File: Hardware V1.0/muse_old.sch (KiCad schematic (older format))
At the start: 47 parts, among them P1 3.5mm_line, P2 3.5mm_line, P3 RCA, P4 RCA, P5 ATX_PWR_OK, P6 ATX_PWR, P7 ATX_GND, P8 ATX_PS_ON, P9 LED_Signal, Q1 FQP30N06L, Q2 FQP30N06L, Q3 FQP30N06L, Q4 FQP30N06L, Q5 FQP30N06L, Q6 FQP30N06L, U1 MSGEQ7, U2 MSGEQ7, U3 74LS595, U4 Spark_Core

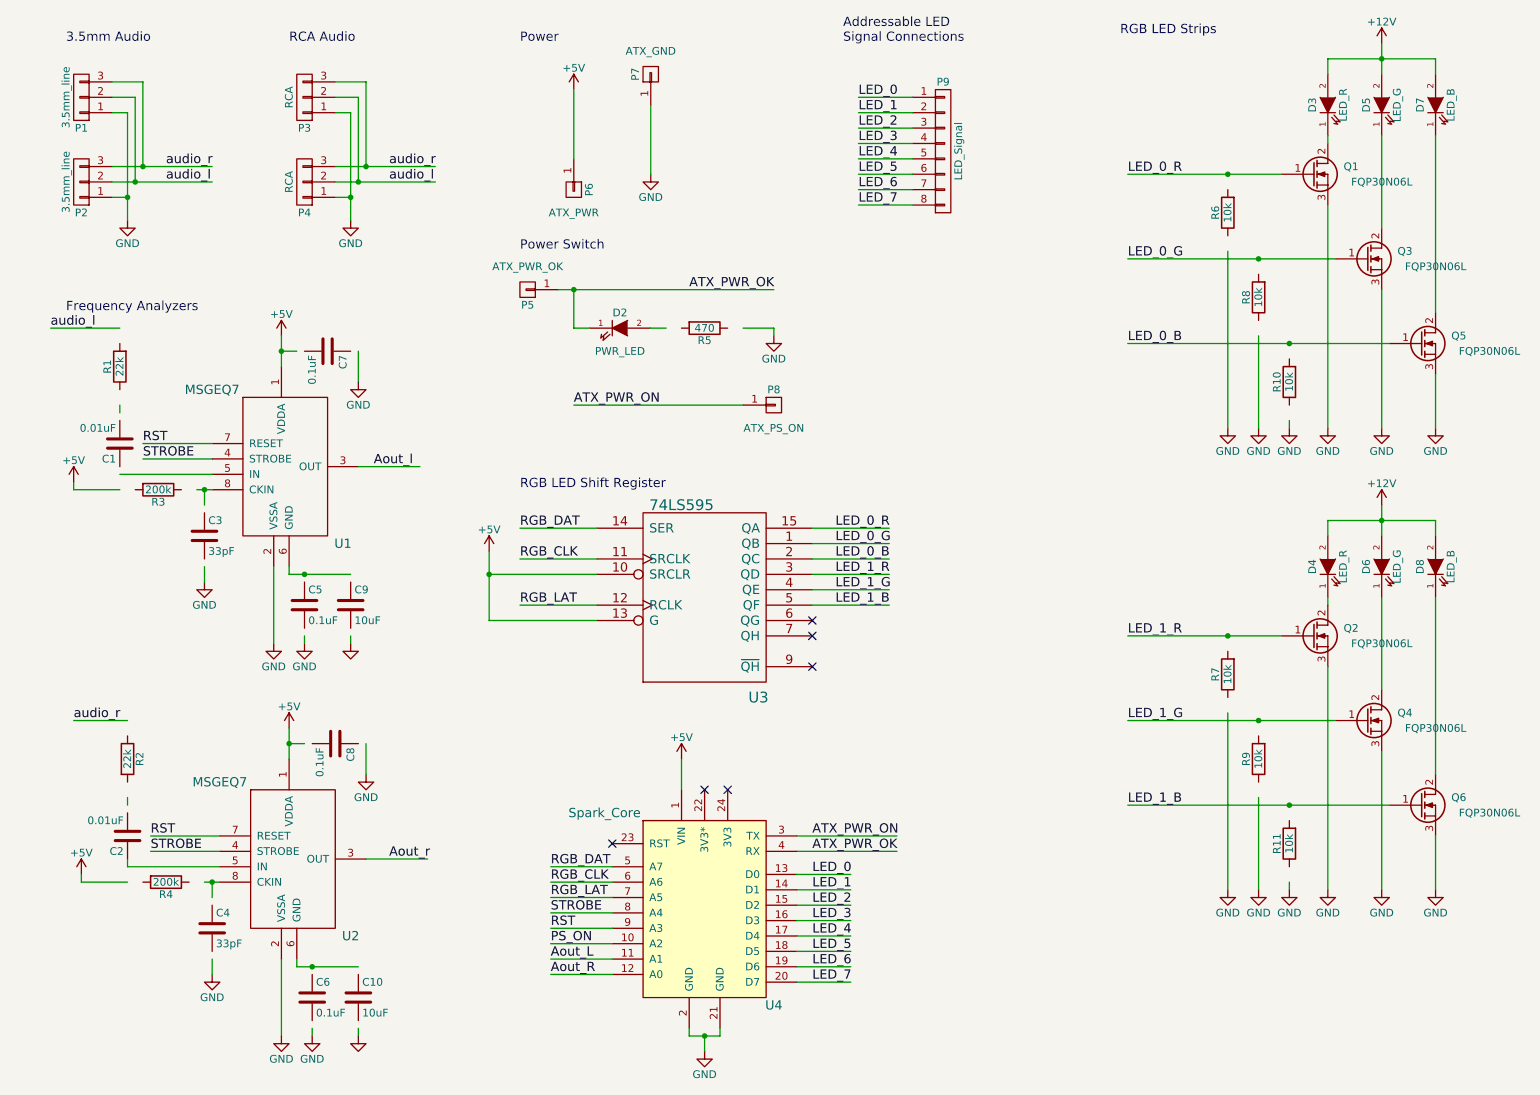
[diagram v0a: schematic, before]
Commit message: Changed versioning scheme. Fixed problems and reuploaded to oshpark
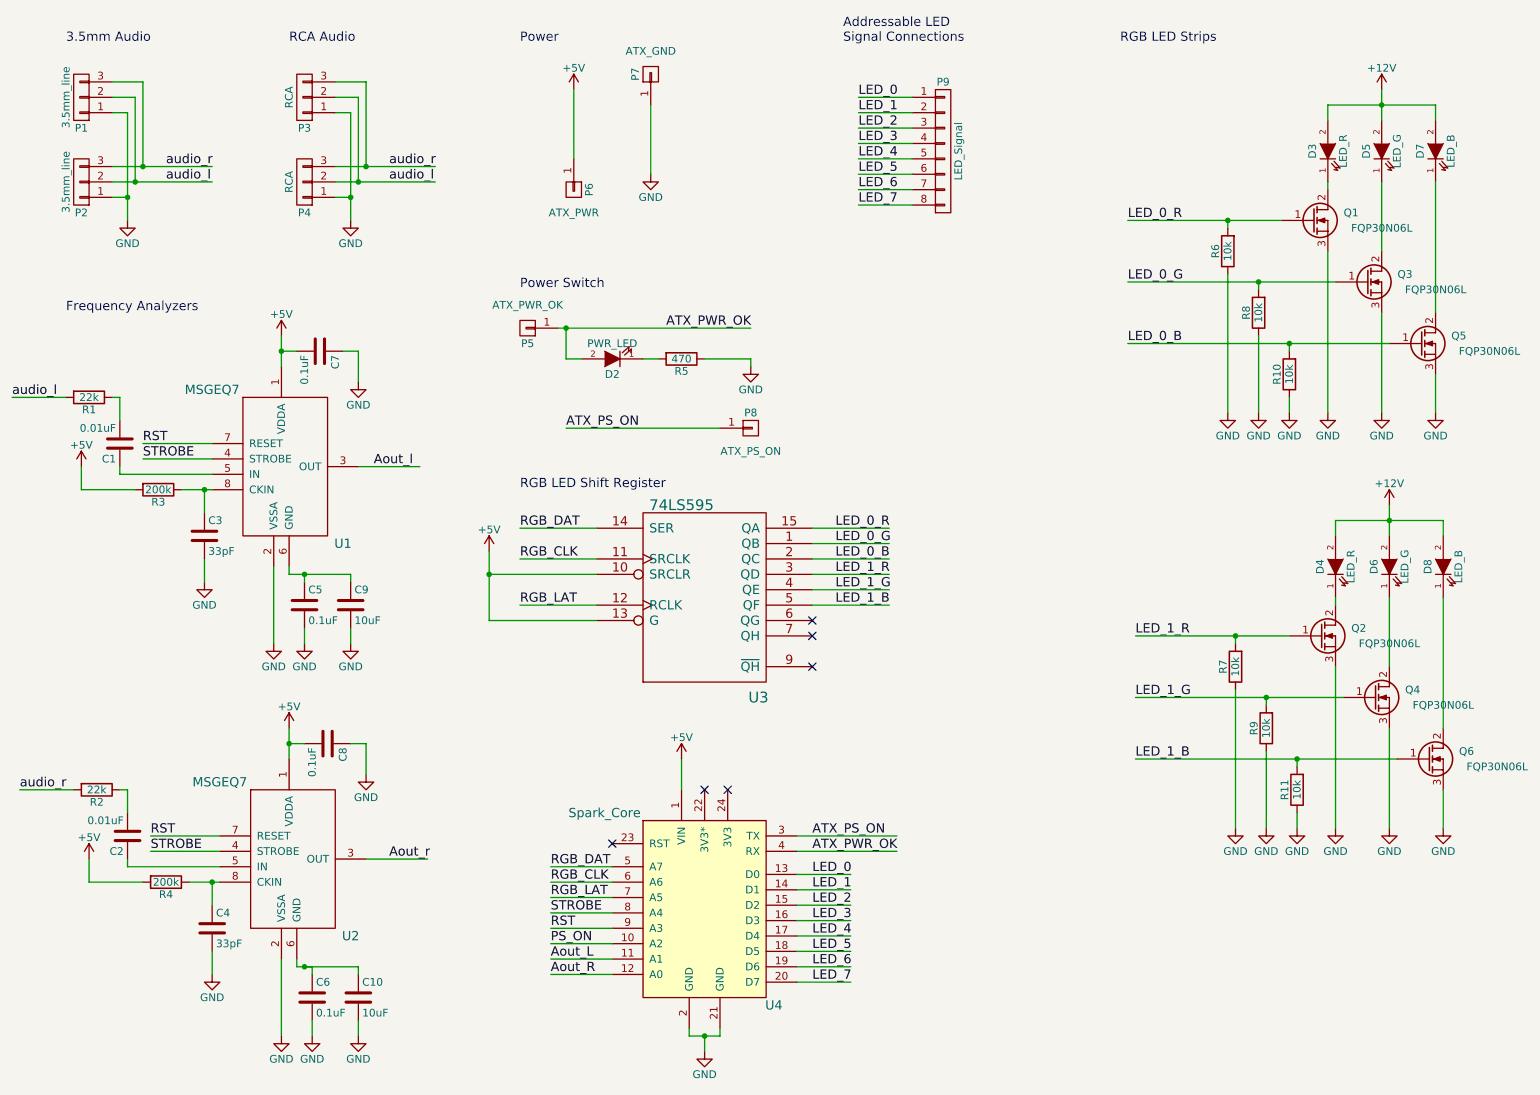
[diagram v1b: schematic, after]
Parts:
- C10, C9: footprint Capacitors_ThroughHole:C_Rect_L7_W2_P5 -> (none)
- Q1, Q2, Q3, Q4, Q5, Q6: footprint TO_SOT_Packages_THT:TO-220_Neutral123_Vertical_LargePads -> Transistors_TO-220:TO-220_Neutral123_Vertical_LargePads
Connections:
- net labels added: ATX_PS_ON
- net labels removed: ATX_PWR_ON
- wire segments 142 -> 157
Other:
- moved on the sheet: C7, C8, D2, D3, D4, D5, D6, D7, D8, P5, P8, Q1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
